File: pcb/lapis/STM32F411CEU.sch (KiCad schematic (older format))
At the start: 11 parts, among them IC5 STM32G484CET6, U1 STM32F411CEUx

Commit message: no message
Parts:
- removed IC5: STM32G484CET6, Package_QFP:LQFP-48_7x7mm_P0.5mm, symbol SamacSys_Parts:STM32G484CET6
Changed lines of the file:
@@
 Text HLabel 7950 5200 2    50   Output ~ 0
 SPEAKER
-$Comp
-L SamacSys_Parts:STM32G484CET6 IC5
-U 1 1 618978F9
-P 9250 3700
-F 0 "IC5" H 10994 3296 50  0000 L CNN
-F 1 "STM32G484CET6" H 10994 3205 50  0000 L CNN
-F 2 "Package_QFP:LQFP-48_7x7mm_P0.5mm" H 10800 4400 50  0001 L CNN
-F 3 "" H 10800 4300 50  0001 L CNN
-F 4 "MCU, 32BIT, 170MHZ, LQFP-48" H 10800 4200 50  0001 L CNN "Description"
-F 5 "1.6" H 10800 4100 50  0001 L CNN "Height"
-F 6 "" H 10800 4000 50  0001 L CNN "RS Part Number"
-F 7 "" H 10800 3900 50  0001 L CNN "RS Price/Stock"
-F 8 "STMicroelectronics" H 10800 3800 50  0001 L CNN "Manufacturer_Name"
-F 9 "STM32G484CET6" H 10800 3700 50  0001 L CNN "Manufacturer_Part_Number"
-	1    9250 3700
-	1    0    0    -1
-$EndComp
 $EndSCHEMATC

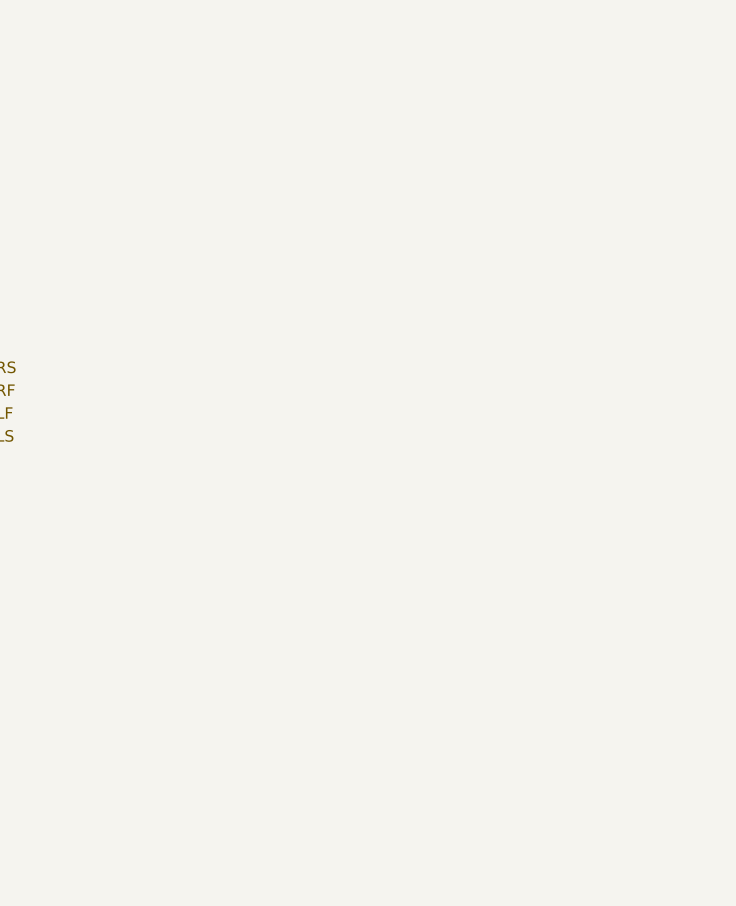
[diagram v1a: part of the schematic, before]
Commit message: STM411失敗基板　STM484に変更し基板修正
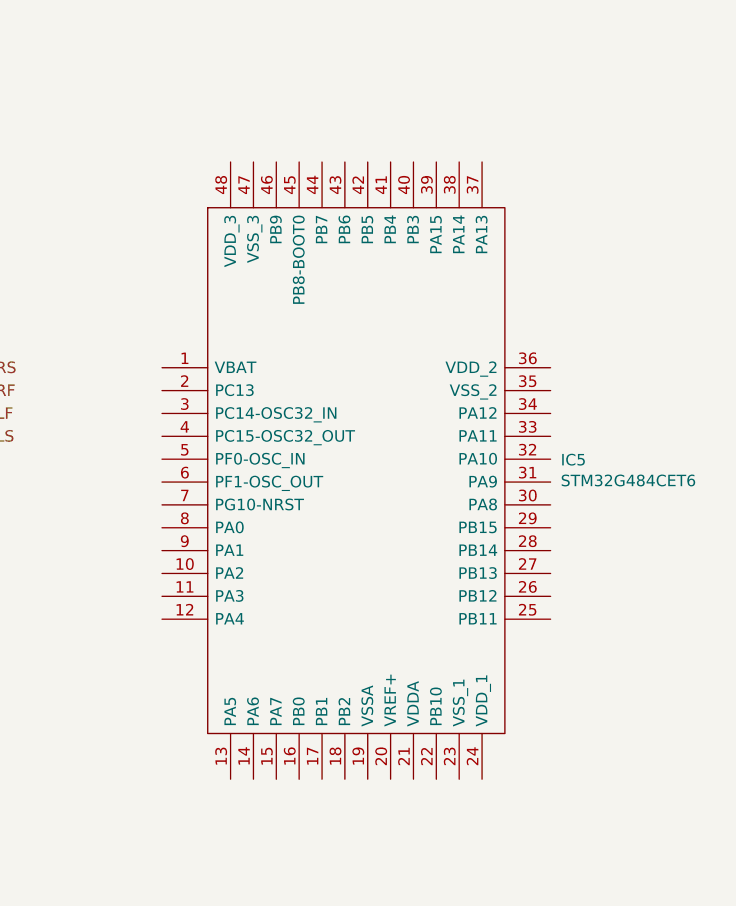
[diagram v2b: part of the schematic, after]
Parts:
- added IC5: STM32G484CET6, Package_QFP:LQFP-48_7x7mm_P0.5mm, symbol SamacSys_Parts:STM32G484CET6
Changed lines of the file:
@@
 Text HLabel 7950 5200 2    50   Output ~ 0
 SPEAKER
+$Comp
+L SamacSys_Parts:STM32G484CET6 IC5
+U 1 1 618978F9
+P 9250 3700
+F 0 "IC5" H 10994 3296 50  0000 L CNN
+F 1 "STM32G484CET6" H 10994 3205 50  0000 L CNN
+F 2 "Package_QFP:LQFP-48_7x7mm_P0.5mm" H 10800 4400 50  0001 L CNN
+F 3 "" H 10800 4300 50  0001 L CNN
+F 4 "MCU, 32BIT, 170MHZ, LQFP-48" H 10800 4200 50  0001 L CNN "Description"
+F 5 "1.6" H 10800 4100 50  0001 L CNN "Height"
+F 6 "" H 10800 4000 50  0001 L CNN "RS Part Number"
+F 7 "" H 10800 3900 50  0001 L CNN "RS Price/Stock"
+F 8 "STMicroelectronics" H 10800 3800 50  0001 L CNN "Manufacturer_Name"
+F 9 "STM32G484CET6" H 10800 3700 50  0001 L CNN "Manufacturer_Part_Number"
+	1    9250 3700
+	1    0    0    -1
+$EndComp
 $EndSCHEMATC
